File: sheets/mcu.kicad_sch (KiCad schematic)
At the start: 7 parts, among them U7 ESP32-WROVER-B

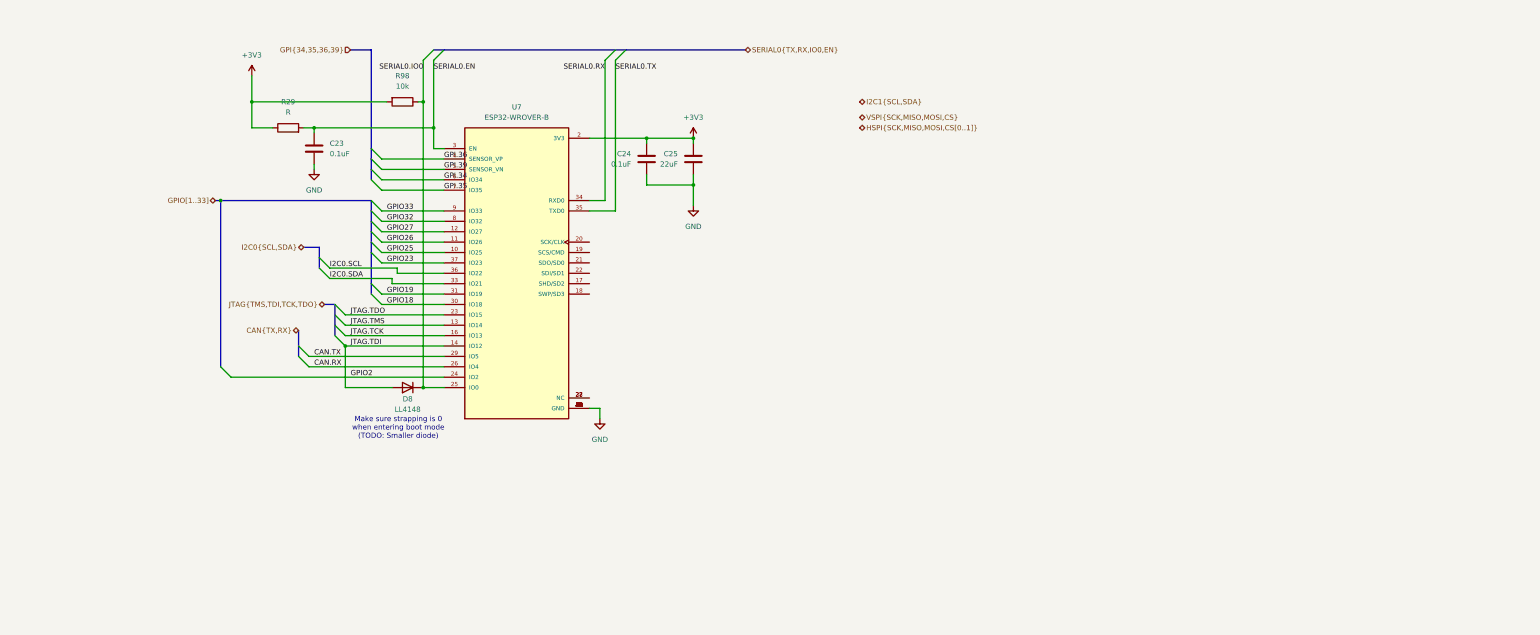
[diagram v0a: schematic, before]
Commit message: add mcu module + position components
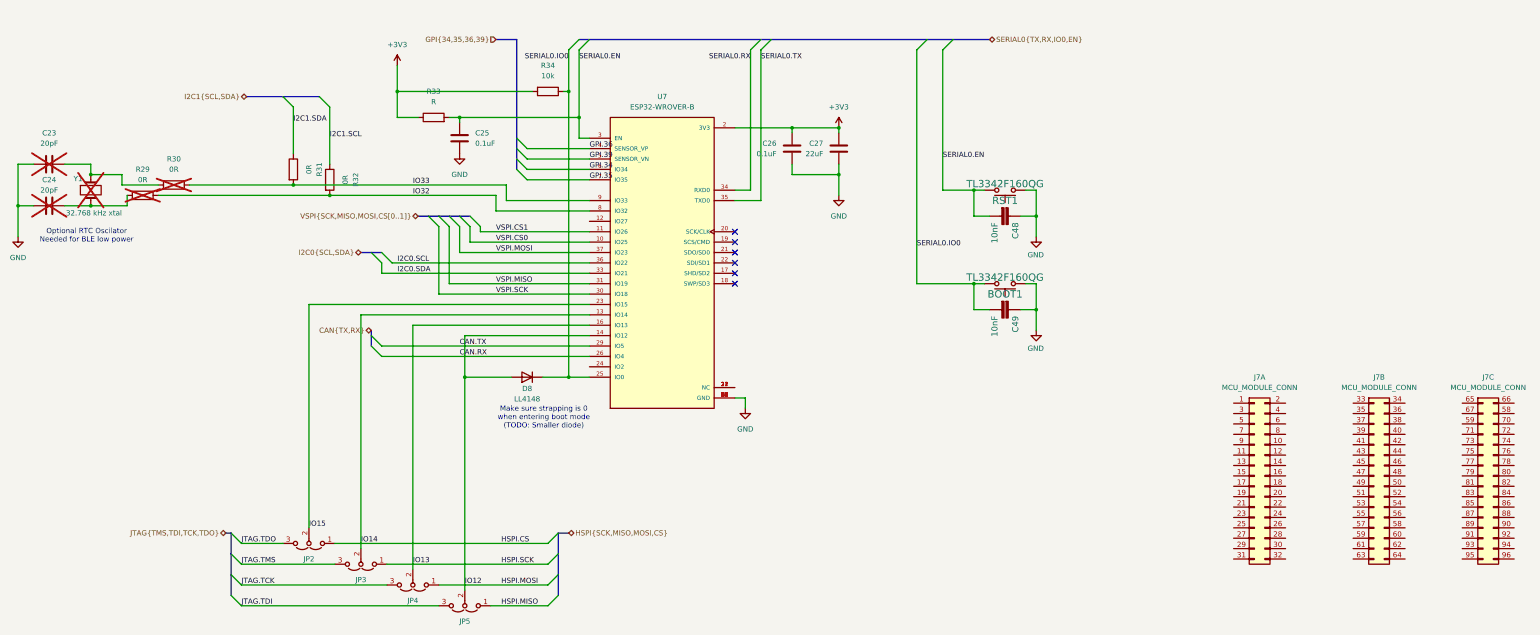
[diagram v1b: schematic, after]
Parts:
- added BOOT1, RST1: TL3342F160QG, Button_Switch_SMD:SW_SPST_TL3342, symbol Switch:SW_Push
- added C23, C24: 20pF, symbol Device:C
- added C48, C49: 10nF, Capacitor_SMD:C_0603_1608Metric, symbol FleetMate_A_Rev03-eagle-import:C-EUC0603
- added J7: MCU_MODULE_CONN, symbol Connectors:MCU_MODULE_CONN
- added JP2, JP3, JP4, JP5: Jumper_3_Open, Connector_PinHeader_2.54mm:PinHeader_1x03_P2.54mm_Vertical, symbol Jumper:Jumper_3_Open
- added R29, R30, R31, R32: 0R, symbol Device:R
- added Y1: 32.768 kHz xtal, symbol Device:Crystal
- renumbered C23 to C25, C24 to C26, C25 to C27, R29 to R33, R98 to R34
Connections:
- net GND: now also BOOT1.2, C23.1, C24.1, C48.1, C49.1, RST1.2
- net JTAG.TCK: now also JP4.3 (B); no longer U7.16 (IO13)
- net JTAG.TDI: now also JP5.3 (B); no longer D8.2 (A), U7.14 (IO12)
- net JTAG.TDO: now also JP2.3 (B); no longer U7.23 (IO15)
- net JTAG.TMS: now also JP3.3 (B); no longer U7.13 (IO14)
- net SERIAL0.EN: now also C48.2, RST1.1
- net SERIAL0.IO0: now also BOOT1.1, C49.2
- net GPIO18 renamed VSPI.SCK
- net GPIO19 renamed VSPI.MISO
- net GPIO2: no longer names the net of U7.24 (IO2)
- net GPIO23 renamed VSPI.MOSI
- net GPIO25 renamed VSPI.CS0
- net GPIO26 renamed VSPI.CS1
- net GPIO27: no longer names the net of U7.12 (IO27)
- net GPIO32 renamed IO32
- net IO32: now also R29.2, R32.2
- net GPIO33 renamed IO33
- net IO33: now also R30.2, R31.2
- new net: C23.2, R30.1, Y1.1
- new net: C24.2, R29.1, Y1.2
- new net HSPI.CS: JP2.1 (A), JP3.2 (C), U7.13 (IO14)
- new net HSPI.MISO: JP5.1 (A)
- new net HSPI.MOSI: D8.2 (A), JP4.1 (A), JP5.2 (C), U7.14 (IO12)
- new net HSPI.SCK: JP3.1 (A), JP4.2 (C), U7.16 (IO13)
- new net I2C1.SCL: R32.1
- new net I2C1.SDA: R31.1
- new net IO15: JP2.2 (C), U7.23 (IO15)
- no-connect marks 0 -> 6
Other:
- note added: "Optional RTC Oscilator Needed for BLE low power"
- moved on the sheet: C25, C26, C27, D8, R33, R34, U7

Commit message: Updated MCU to MCU module + set SMD comp. footprints
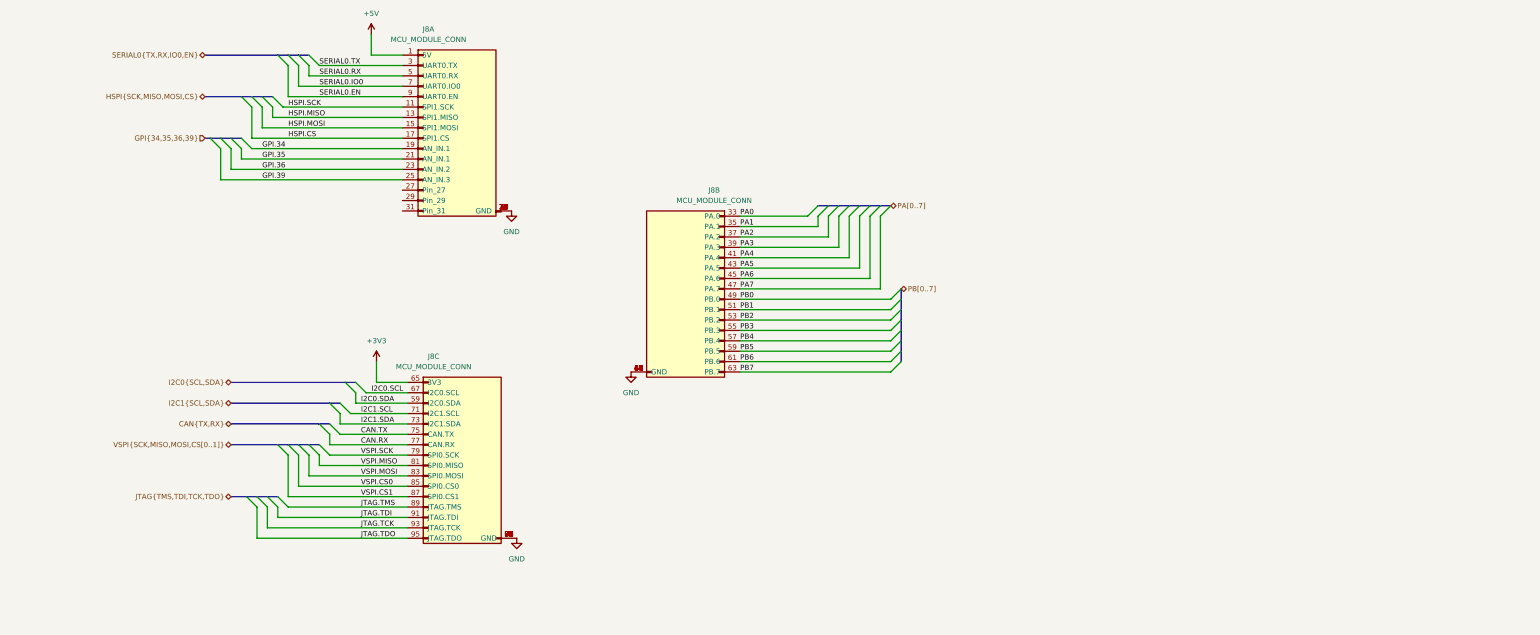
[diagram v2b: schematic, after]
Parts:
- removed BOOT1, RST1: TL3342F160QG, Button_Switch_SMD:SW_SPST_TL3342, symbol Switch:SW_Push
- removed C23, C24: 20pF, symbol Device:C
- removed C25, C26: 0.1uF, symbol Device:C
- removed C27: 22uF, symbol Device:C
- removed C48, C49: 10nF, Capacitor_SMD:C_0603_1608Metric, symbol FleetMate_A_Rev03-eagle-import:C-EUC0603
- removed D8: LL4148, Diode_SMD:D_MiniMELF, symbol Diode:LL4148
- removed J7: MCU_MODULE_CONN, symbol Connectors:MCU_MODULE_CONN
- removed JP2, JP3, JP4, JP5: Jumper_3_Open, Connector_PinHeader_2.54mm:PinHeader_1x03_P2.54mm_Vertical, symbol Jumper:Jumper_3_Open
- removed R29, R30, R31, R32: 0R, symbol Device:R
- removed R33: R, symbol Device:R
- removed R34: 10k, symbol Device:R
- removed U7: ESP32-WROVER-B, ICs:MODULE_ESP32-WROVER-B, symbol ICs:ESP32-WROVER-B
- removed Y1: 32.768 kHz xtal, symbol Device:Crystal
- added J8: MCU_MODULE_CONN, Connectors:mcu_conn, symbol Connectors:MCU_MODULE_CONN
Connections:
- net +3V3: now also J8.65 (3V3)
- net CAN.RX: now also J8.77 (CAN.RX)
- net CAN.TX: now also J8.75 (CAN.TX)
- net GND: now also J8.10 (GND), J8.12 (GND), J8.14 (GND), J8.16 (GND), J8.18 (GND), J8.2 (GND), J8.20 (GND), J8.22 (GND), J8.24 (GND), J8.26 (GND), J8.28 (GND), J8.30 (GND), J8.32 (GND), J8.34 (GND), J8.36 (GND), J8.38 (GND), J8.4 (GND), J8.40 (GND), J8.42 (GND), J8.44 (GND), J8.46 (GND), J8.48 (GND), J8.50 (GND), J8.52 (GND), J8.54 (GND), J8.56 (GND), J8.58 (GND), J8.58 (GND), J8.6 (GND), J8.60 (GND), J8.62 (GND), J8.64 (GND), J8.66 (GND), J8.70 (GND), J8.72 (GND), J8.74 (GND), J8.76 (GND), J8.78 (GND), J8.8 (GND), J8.80 (GND), J8.82 (GND), J8.84 (GND), J8.86 (GND), J8.88 (GND), J8.90 (GND), J8.92 (GND), J8.94 (GND), J8.96 (GND)
- net GPI.34: now also J8.19 (AN_IN.1)
- net GPI.35: now also J8.21 (AN_IN.1)
- net GPI.36: now also J8.23 (AN_IN.2)
- net GPI.39: now also J8.25 (AN_IN.3)
- net HSPI.CS: now also J8.17 (SPI1.CS)
- net HSPI.MISO: now also J8.13 (SPI1.MISO)
- net HSPI.MOSI: now also J8.15 (SPI1.MOSI)
- net HSPI.SCK: now also J8.11 (SPI1.SCK)
- net I2C0.SCL: now also J8.67 (I2C0.SCL)
- net I2C0.SDA: now also J8.59 (I2C0.SDA)
- net I2C1.SCL: now also J8.71 (I2C1.SCL)
- net I2C1.SDA: now also J8.73 (I2C1.SDA)
- net JTAG.TCK: now also J8.93 (JTAG.TCK)
- net JTAG.TDI: now also J8.91 (JTAG.TDI)
- net JTAG.TDO: now also J8.95 (JTAG.TDO)
- net JTAG.TMS: now also J8.89 (JTAG.TMS)
- net SERIAL0.EN: now also J8.9 (UART0.EN)
- net SERIAL0.IO0: now also J8.7 (UART0.IO0)
- net SERIAL0.RX: now also J8.5 (UART0.RX)
- net SERIAL0.TX: now also J8.3 (UART0.TX)
- net VSPI.CS0: now also J8.85 (SPI0.CS0)
- net VSPI.CS1: now also J8.87 (SPI0.CS1)
- net VSPI.MISO: now also J8.81 (SPI0.MISO)
- net VSPI.MOSI: now also J8.83 (SPI0.MOSI)
- net VSPI.SCK: now also J8.79 (SPI0.SCK)
- new net +5V: J8.1 (5V)
- new net PA0: J8.33 (PA.0)
- new net PA1: J8.35 (PA.1)
- new net PA2: J8.37 (PA.2)
- new net PA3: J8.39 (PA.3)
- new net PA4: J8.41 (PA.4)
- new net PA5: J8.43 (PA.5)
- new net PA6: J8.45 (PA.6)
- new net PA7: J8.47 (PA.7)
- new net PB0: J8.49 (PB.0)
- new net PB1: J8.51 (PB.1)
- new net PB2: J8.53 (PB.2)
- new net PB3: J8.55 (PB.3)
- new net PB4: J8.57 (PB.4)
- new net PB5: J8.59 (PB.5)
- new net PB6: J8.61 (PB.6)
- new net PB7: J8.63 (PB.7)
- no-connect marks 6 -> 0
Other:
- note removed: "Make sure strapping is 0 when entering boot mode (TODO: Smaller diode)"
- note removed: "Optional RTC Oscilator Needed for BLE low power"

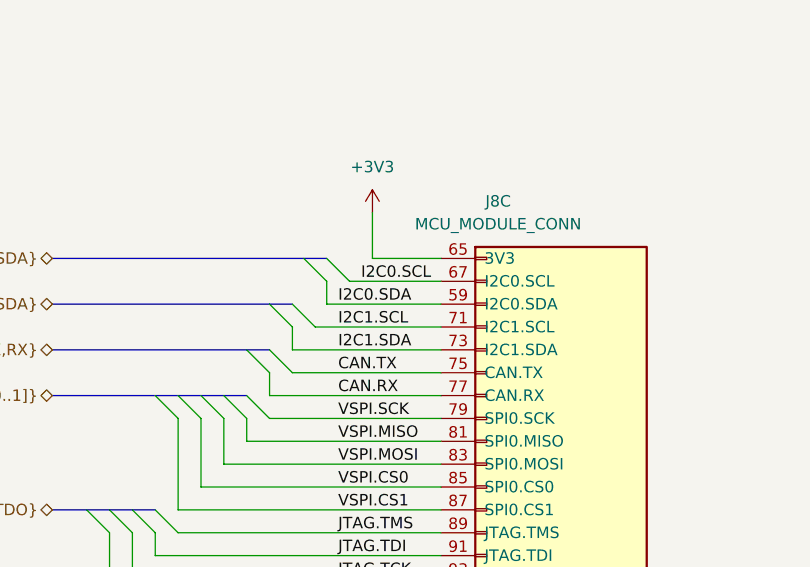
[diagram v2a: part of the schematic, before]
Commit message: routed buses
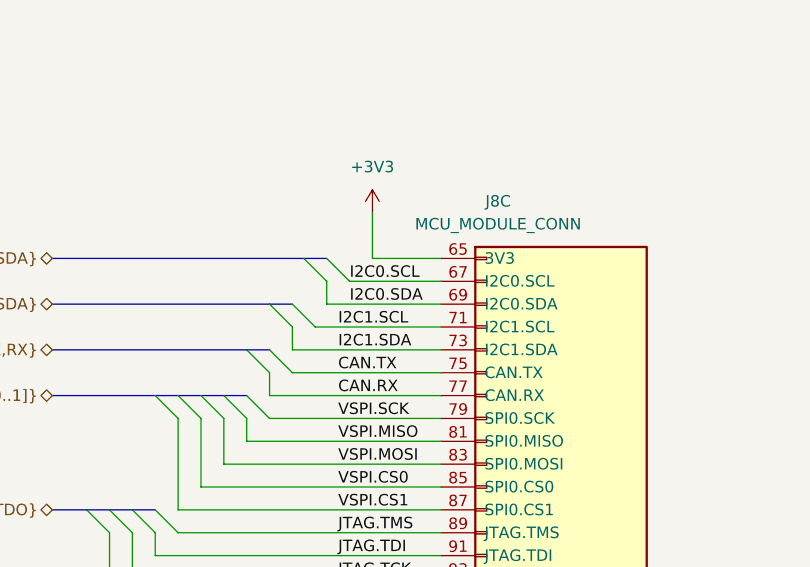
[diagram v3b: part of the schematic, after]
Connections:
- net I2C0.SDA: now also J8.69 (I2C0.SDA); no longer J8.59 (I2C0.SDA)
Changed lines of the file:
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@@
 	)
 	(label "I2C0.SCL"
-		(at 106.68 119.38 0)
+		(at 105.41 119.38 0)
 		(effects
 			(font
@@
 	)
 	(label "I2C0.SDA"
-		(at 104.14 121.92 0)
+		(at 105.41 121.92 0)
 		(effects
 			(font
@@
 	)
 	(symbol
+		(lib_name "MCU_MODULE_CONN_1")
 		(lib_id "Connectors:MCU_MODULE_CONN")
 		(at 120.65 134.62 0)
@@
 		(pin "38"
 		)
-		(pin "59"
+		(pin "69"
 		)
 		(pin "57"
